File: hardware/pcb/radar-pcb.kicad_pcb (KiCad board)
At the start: 2 copper layers, 66 x 91 mm, 71 parts, among them J1 USB-C zasilanie 5 V (GCT USB4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, J10 Awaryjne wgrywanie: BOOT GND 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, J2 DevKit J1, J3 DevKit J3, J4 HC-SR04 (kabel): VCC TRIG ECH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, J5 Serwo SG90 (kabel): GND +5V S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, J6 MAX7219 Elegoo: VCC GND DIN C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, J7 OLED SH1106: VCC GND SCK SDA, J8 Buzzer: + -, J9 Przycisk zewnetrzny, Q2 MMBT3904, SW1 Przycisk ON/standby (katowy), U1 SN74AHCT125D, U2 AP22802AW5-7 (przelacznik 5 V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

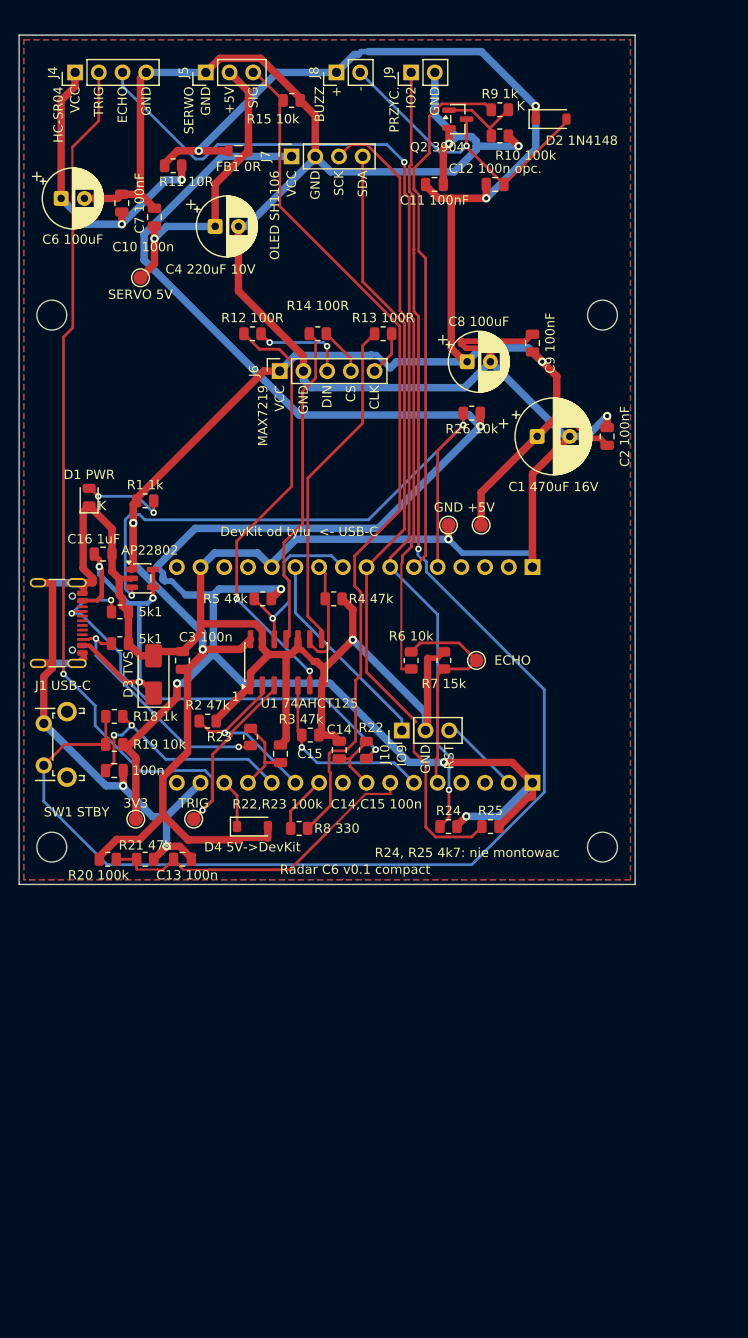
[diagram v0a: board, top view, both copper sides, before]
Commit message: PCB: USB-C zmienione na HRO TYPE-C-31-M-12 (LCSC C165948), BOM z C96346 dla 100 kΩ
GCT USB4105-GF-A był niedostępny w JLCPCB. Nowy footprint z biblioteki KiCad, gniazdo
przesunięte o 0,36 mm ku krawędzi (x = 2,74), usunięte dwa odcinki obrysu silkscreenu przy
krawędzi. Pełny build: ERC 0 błędów, DRC 0 błędów i 0 niepołączonych, 0 niezgodności ze
schematem, jedno ostrzeżenie lib_footprint_mismatch (celowa zmiana obrysu). Odświeżone rendery
i pliki produkcyjne. Nie sprawdzone na sprzęcie.

Co-Authored-By: Claude Sonnet 5.5 <noreply@anthropic.com>
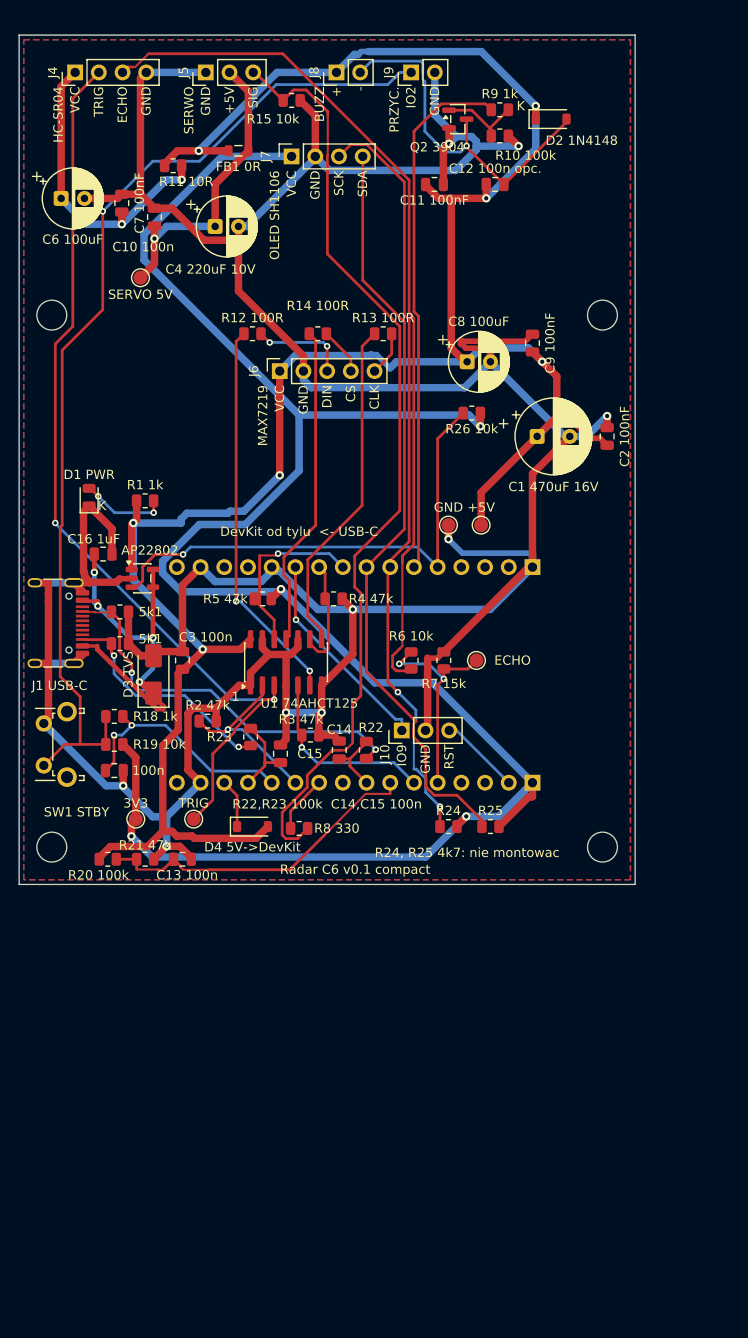
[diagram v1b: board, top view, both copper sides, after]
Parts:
- J1: value USB-C zasilanie 5 V (GCT USB4105) -> USB-C zasilanie 5 V (HRO TYPE-C-31-M-12); footprint Connector_USB:USB_C_Receptacle_GCT_USB4105-xx-A_16P_TopMnt_Horizontal -> Connector_USB:USB_C_Receptacle_HRO_TYPE-C-31-M-12
- moved J1 0.36 mm to (102.7, 88.0)
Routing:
- net BTN: track 157.4 -> 109.7 mm
- net U2_FLG: track 67.8 -> 54.0 mm, vias 2 -> 1
- net TRIG_5V: track 109.8 -> 100.0 mm
- net VIN: track 36.4 -> 45.6 mm, vias 3 -> 4
- net GND: track 418.2 -> 427.3 mm, vias 7 -> 9
- net SERVO_SIG: track 93.5 -> 101.3 mm
- net +5V: track 245.5 -> 252.4 mm, vias 6 -> 7
- net CC1: track 48.6 -> 42.3 mm, vias 3 -> 2
- net DIN_5V: track 46.8 -> 41.5 mm
- net BUZ_NEG: track 33.6 -> 38.8 mm
- net SDA: track 85.1 -> 82.1 mm
- net CC2: track 25.9 -> 24.6 mm
- net ECHO_3V3: track 24.7 -> 23.6 mm, vias 0 -> 2
- net +3V3: track 210.1 -> 209.1 mm, vias 5 -> 4
- net BUZ_CTRL: track 57.5 -> 56.9 mm
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
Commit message: PCB v0.2: wersja przewlekana (gniazdo DC, PTC + TVS, DIP-14), piny DevKita na listwach, pole prototypowe; firmware bez CC/FLG
Wszystko do ręcznego lutowania, płytki zamawiane bez montażu. Rozmieszczenie automatyczne
(tools/autoplace.py, geom.py), płytka 76 x 137,5 mm. J11/J12 = kopie wszystkich pinów DevKita,
J13 = listwa GND/3V3/5V, 4 bloki 2x14 = pole prototypowe. Miejsce na logo (footprint z Image Convertera)
w prawym dolnym rogu. POWER_MONITOR_USB_C=0 w firmware (tylko pomiar 5 V). Lista zakupów i Gerbery
w production/. ERC 0 błędów; DRC 0 błędów, 0 niepołączonych, 0 niezgodności ze schematem
(5 ostrzeżeń lib_footprint_mismatch: celowo uproszczone J1 i J14-J17). pio run przechodzi.
Nic nie sprawdzono na sprzęcie.

Co-Authored-By: Claude Sonnet 5.5 <noreply@anthropic.com>
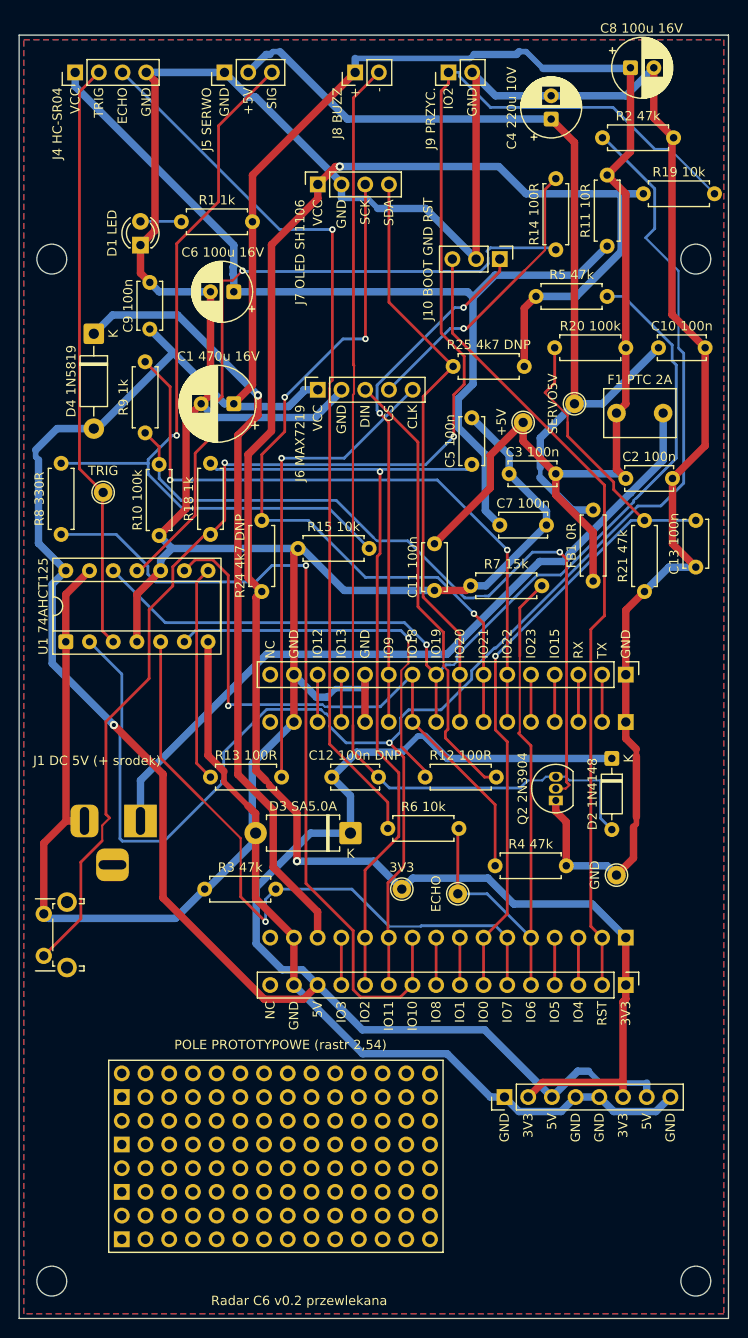
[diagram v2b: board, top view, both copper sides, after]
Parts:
- removed C14, C15: 100 nF, Capacitor_SMD:C_0805_2012Metric
- removed C16: 1 uF, Capacitor_SMD:C_0805_2012Metric
- removed R16, R17: 5,1 k, Resistor_SMD:R_0805_2012Metric
- removed R22, R23: 100 k, Resistor_SMD:R_0805_2012Metric
- removed R26: 10 k, Resistor_SMD:R_0805_2012Metric
- removed U2: AP22802AW5-7 (przelacznik 5 V, LCSC C211404, limit ok. 2,2-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, Package_TO_SOT_SMD:SOT-23-5
- added F1: PTC 2 A (hold), rastr 5 mm, Capacitor_THT:C_Disc_D7.5mm_W5.0mm_P5.00mm, F.Cu at (169.0, 65.5)
- added J11: Piny DevKit J3 (kopia J3), Connector_PinHeader_2.54mm:PinHeader_1x16_P2.54mm_Vertical, F.Cu at (165.0, 93.5)
- added J12: Piny DevKit J1 (kopia J2), Connector_PinHeader_2.54mm:PinHeader_1x16_P2.54mm_Vertical, F.Cu at (165.0, 126.8)
- added J13: Listwa zasilania: GND 3V3 5V, Connector_PinHeader_2.54mm:PinHeader_1x08_P2.54mm_Vertical, F.Cu at (152.0, 138.8)
- added J14: Pole prototypowe 1 (2x14, niepodlaczone), Connector_PinHeader_2.54mm:PinHeader_2x14_P2.54mm_Vertical, F.Cu at (111.0, 138.8)
- added J15: Pole prototypowe 2 (2x14, niepodlaczone), Connector_PinHeader_2.54mm:PinHeader_2x14_P2.54mm_Vertical, F.Cu at (111.0, 143.9)
- added J16: Pole prototypowe 3 (2x14, niepodlaczone), Connector_PinHeader_2.54mm:PinHeader_2x14_P2.54mm_Vertical, F.Cu at (111.0, 148.9)
- added J17: Pole prototypowe 4 (2x14, niepodlaczone), Connector_PinHeader_2.54mm:PinHeader_2x14_P2.54mm_Vertical, F.Cu at (111.0, 154.0)
- C10, C11, C12, C13, C2, C3, C5, C7, C9: footprint Capacitor_SMD:C_0805_2012Metric -> Capacitor_THT:C_Disc_D5.0mm_W2.5mm_P5.00mm
- D1: value LED zasilania -> LED zasilania 3 mm; footprint LED_SMD:LED_0805_2012Metric -> LED_THT:LED_D3.0mm
- D2: value 1N4148W -> 1N4148; footprint Diode_SMD:D_SOD-123 -> Diode_THT:D_DO-35_SOD27_P7.62mm_Horizontal
- D3: value SMAJ5.0A (TVS 5 V, jednokierunkowy) -> TVS SA5.0A (DO-15, katoda do +5V); footprint Diode_SMD:D_SMA -> Diode_THT:D_DO-15_P10.16mm_Horizontal
- D4: value 1N5819HW -> 1N5819; footprint Diode_SMD:D_SOD-123 -> Diode_THT:D_DO-41_SOD81_P10.16mm_Horizontal
- FB1: value 0 R (zworka; opcja: ferryt >= 1 A) -> 0 R (zworka z drutu; opcja: ferryt >= 1 A); footprint Inductor_SMD:L_0805_2012Metric -> Resistor_THT:R_Axial_DIN0207_L6.3mm_D2.5mm_P7.62mm_Horizontal
- J1: value USB-C zasilanie 5 V (HRO TYPE-C-31-M-12) -> Gniazdo DC 5,5/2,1 mm, srodek +5 V; footprint Connector_USB:USB_C_Receptacle_HRO_TYPE-C-31-M-12 -> Connector_BarrelJack:BarrelJack_Horizontal
- Q2: value MMBT3904 -> 2N3904 (TO-92, E B C); footprint Package_TO_SOT_SMD:SOT-23 -> Package_TO_SOT_THT:TO-92_Inline
- R1, R10, R11, R12, R13, R14, R15, R18, R19, R2, R20, R21, R24, R25, R3, R4, R5, R6, R7, R8, R9: footprint Resistor_SMD:R_0805_2012Metric -> Resistor_THT:R_Axial_DIN0207_L6.3mm_D2.5mm_P7.62mm_Horizontal
- TP1, TP2, TP3, TP4, TP5, TP6: footprint TestPoint:TestPoint_Pad_D1.5mm -> TestPoint:TestPoint_THTPad_D2.0mm_Drill1.0mm
- U1: value SN74AHCT125D -> SN74AHCT125N (DIP-14); footprint Package_SO:SOIC-14_3.9x8.7mm_P1.27mm -> Package_DIP:DIP-14_W7.62mm_Socket
- moved R19 87.3 mm to (174.5, 42.0), turned to 180 degrees
- moved R20 78.0 mm to (165.0, 58.5), turned to 180 degrees
- moved R2 75.5 mm to (162.5, 36.0)
- moved Q2 73.8 mm to (157.5, 107.0), turned to 90 degrees
- moved D2 68.8 mm to (163.5, 102.5), turned to -90 degrees
- moved C13 65.9 mm to (172.5, 77.0), turned to -90 degrees
- moved C12 65.9 mm to (133.5, 104.5)
- moved R21 64.7 mm to (167.0, 77.0), turned to -90 degrees
- moved FB1 59.7 mm to (161.5, 83.5), turned to 90 degrees
- moved C10 55.8 mm to (168.5, 58.5), turned to 0 degrees
- moved D4 55.5 mm to (108.0, 57.0), turned to -90 degrees
- moved C7 53.2 mm to (151.5, 77.5), turned to 0 degrees
- moved J10 51.6 mm to (151.5, 49.0), turned to -90 degrees
- moved R12 51.0 mm to (143.5, 104.5)
- moved R13 51.0 mm to (120.5, 104.5)
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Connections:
- D3 pad 1: VIN -> +5V
- J2 pad 13: CC2_SENSE -> IO3
- J2 pad 3: unconnected-(J2-Pin_3-Pad3) -> IO4
- J2 pad 4: unconnected-(J2-Pin_4-Pad4) -> IO5
- J2 pad 8: CC1_SENSE -> IO1
- J2 pad 9: unconnected-(J2-Pin_9-Pad9) -> IO8
- J3 pad 13: unconnected-(J3-Pin_13-Pad13) -> IO13
- J3 pad 14: unconnected-(J3-Pin_14-Pad14) -> IO12
- J3 pad 2: unconnected-(J3-Pin_2-Pad2) -> TX
- J3 pad 3: unconnected-(J3-Pin_3-Pad3) -> RX
- J3 pad 4: unconnected-(J3-Pin_4-Pad4) -> IO15
- J3 pad 5: U2_FLG -> IO23
- Q2 pad 1: BUZ_BASE -> GND
- Q2 pad 2: GND -> BUZ_BASE
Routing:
- net TRIG_3V3: track 19.5 -> 174.7 mm
- net +5V: track 252.4 -> 392.3 mm, vias 7 -> 1
- net GND: track 427.3 -> 551.4 mm, vias 9 -> 0
- net SERVO_3V3: track 6.16 -> 89.4 mm, vias 0 -> 1
- net CS_3V3: track 19.8 -> 102.8 mm
- net DEVKIT_5V: track 5.27 -> 84.5 mm, vias 0 -> 1
- net EN: track 8.70 -> 85.6 mm
- net BUZ_BASE: track 8.85 -> 82.7 mm, vias 0 -> 1
- net BUZ_NEG: track 38.8 -> 108.6 mm, vias 1 -> 0
- net SR04_VCC: track 33.0 -> 100.0 mm, vias 2 -> 0
- net SERVO_5V: track 32.0 -> 96.0 mm, vias 1 -> 0
- net BTN_ESP: track 25.4 -> 86.3 mm, vias 2 -> 1
- net U2_FLG: track 54.0 -> 0.00 mm, vias 1 -> 0
- net CLK_3V3: track 12.1 -> 65.3 mm, vias 0 -> 1
- net BTN: track 109.7 -> 162.4 mm, vias 1 -> 2
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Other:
- board size 66 x 91 mm -> 76 x 137.5 mm
- board text added: "C1 470u 16V"
- board text added: "C11 100n"
- board text added: "C12 100n DNP"
- board text added: "C2 100n"
- board text added: "C4 220u 10V"
- board text added: "C5 100n"
- board text added: "C6 100u 16V"
- board text added: "C7 100n"
- board text added: "C8 100u 16V"
- board text added: "C9 100n"
- board text added: "D1 LED"
- board text added: "D3 SA5.0A"
- board text added: "D4 1N5819"
- board text added: "F1 PTC 2A"
- board text added: "J1 DC 5V (+ srodek)"
- board text added: "J10 BOOT GND RST"
- board text added: "J4 HC-SR04"
- board text added: "J5 SERWO"
- board text added: "J6 MAX7219"
- board text added: "J7 OLED SH1106"
- board text added: "J8 BUZZ"
- board text added: "J9 PRZYC."
- board text added: "POLE PROTOTYPOWE (rastr 2,54)"
- board text added: "Projekt roboczy v0.2 (przewlekany) - NIE ZAMAWIAC przed weryfikacja wymiarow."
- board text added: "Q2 2N3904"
- board text added: "R24 4k7 DNP"
- board text added: "R25 4k7 DNP"
- board text added: "R8 330R"
- board text added: "Radar C6 v0.2 przewlekana"
- board text added: "Radar ESP32-C6 - tyl, DevKit USB-C ->"
- board text added: "SERVO5V"
- board text added: "W1 szerokosc plytki: czy miesci sie we wnetrzu obudowy"
- board text added: "W2 wysokosc plytki (wersja przewlekana, z polem prototypowym)"
- board text added: "W6 gniazdo DC: od gornej krawedzi do osi wtyku (otwor w scianie obudowy)"
- board text added: "WYMIARY DO WERYFIKACJI (? = do potwierdzenia, OK = zmierzone)"
- board text removed: "1"
- board text removed: "100n"
- board text removed: "5k1"
- board text removed: "AP22802"
- board text removed: "BUZZ"
- board text removed: "C1 470uF 16V"
- board text removed: "C11 100nF"
- board text removed: "C12 100n opc."
- board text removed: "C14"
- board text removed: "C15"
- board text removed: "C16 1uF"
- board text removed: "C2 100nF"
- board text removed: "C4 220uF 10V"
- board text removed: "C6 100uF"
- board text removed: "C7 100nF"
- board text removed: "C8 100uF"
- board text removed: "C9 100nF"
- board text removed: "D1 PWR"
- board text removed: "D3 TVS"
- board text removed: "D4 5V->DevKit"
- board text removed: "DevKit J1 (pin 1 = 3V3)"
- board text removed: "DevKit J3 (pin 1 = GND)"
- board text removed: "DevKit od tylu <- USB-C"
- board text removed: "HC-SR04"
- board text removed: "J1 USB-C"
- board text removed: "J10"
- board text removed: "K"
- board text removed: "MAX7219"
- board text removed: "OLED SH1106"
- board text removed: "PRZYC."
- board text removed: "Projekt roboczy v0.1 - NIE ZAMAWIAC przed weryfikacja wymiarow."
- board text removed: "Q2 3904"
- board text removed: "R22"
- board text removed: "R22,R23 100k C14,C15 100n"
- board text removed: "R23"
- board text removed: "R24"
- board text removed: "R24, R25 4k7: nie montowac"
- board text removed: "R25"
- board text removed: "R26 10k"
- board text removed: "R8 330"
- board text removed: "Radar C6 v0.1 compact"
- board text removed: "Radar ESP32-C6 - tyl"
- board text removed: "SERVO 5V"
- board text removed: "SERWO"
- board text removed: "SW1 STBY"
- board text removed: "USB-C ->"
- board text removed: "W1 szerokosc plytki: czy miesci sie we wnetrzu kolumny obudowy"
- board text removed: "W2 wysokosc plytki (wariant kompaktowy, moduly na kablach)"
- board text removed: "W3 gniazdo kabla OLED (J7): od lewej krawedzi do pinu 1"
- board text removed: "W4 gniazdo kabla MAX7219 (J6): od lewej krawedzi do pinu 1"
- board text removed: "W6 gniazdo USB-C zasilania: od gornej krawedzi do osi wtyku (otwor w scianie obudowy)"
- board text removed: "WYMIARY DO WERYFIKACJI (? = do potwierdzenia, OK = zmierzone lub zatwierdzone 2026-10-13)"

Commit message: PCB v0.2: logo Adam & Mateusz na silkscreenie (prawy dolny róg)
logo_trace.py wektoryzuje logo/am-logo-source.jfif (kontury, gładkie krawędzie, otwory w literach),
logo_footprint.py zapisuje footprint logo/am-logo.kicad_mod na F.SilkS (odpowiednik Image Convertera),
gen_pcb.py ustawia go w obszarze G.LOGO. Płytka 76 x 137,5 mm, DRC bez błędów (0 niepołączonych).
Odświeżone rendery i Gerbery. Nic nie sprawdzono na sprzęcie.

Co-Authored-By: Claude Sonnet 5.5 <noreply@anthropic.com>
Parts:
- added LOGO: am-logo, am-logo, F.Cu at (158.0, 153.4)

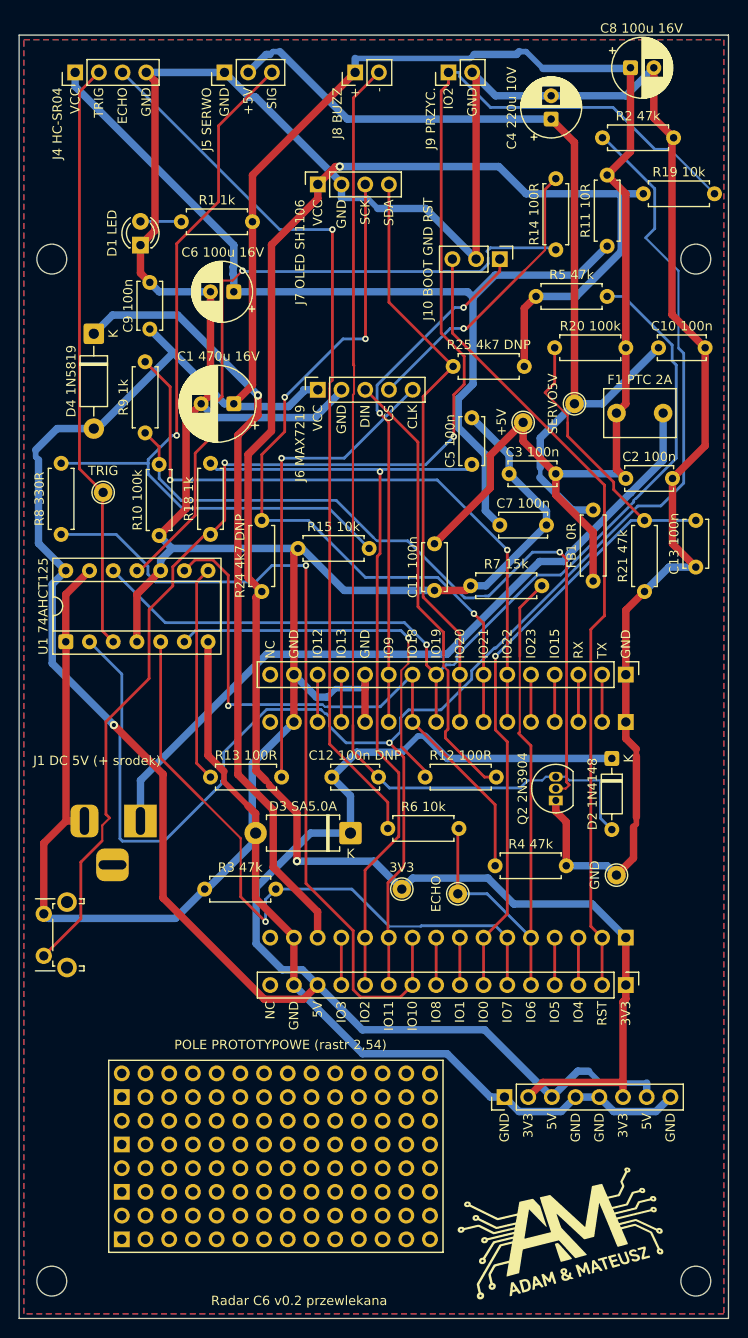
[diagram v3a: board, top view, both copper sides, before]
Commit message: PCB v0.2: wszystkie listwy żeńskie (J4-J13)
Listwy J4, J5, J8, J9, J10, J11, J12 i J13 zmienione z goldpinów na gniazda żeńskie (ten sam rozstaw
i numeracja pinów, układ i trasowanie bez zmian). Lista zakupów i notatki zaktualizowane.
ERC 0 błędów; DRC 0 błędów, 0 niepołączonych, 0 niezgodności ze schematem. Nic nie sprawdzono na sprzęcie.

Co-Authored-By: Claude Sonnet 5.5 <noreply@anthropic.com>
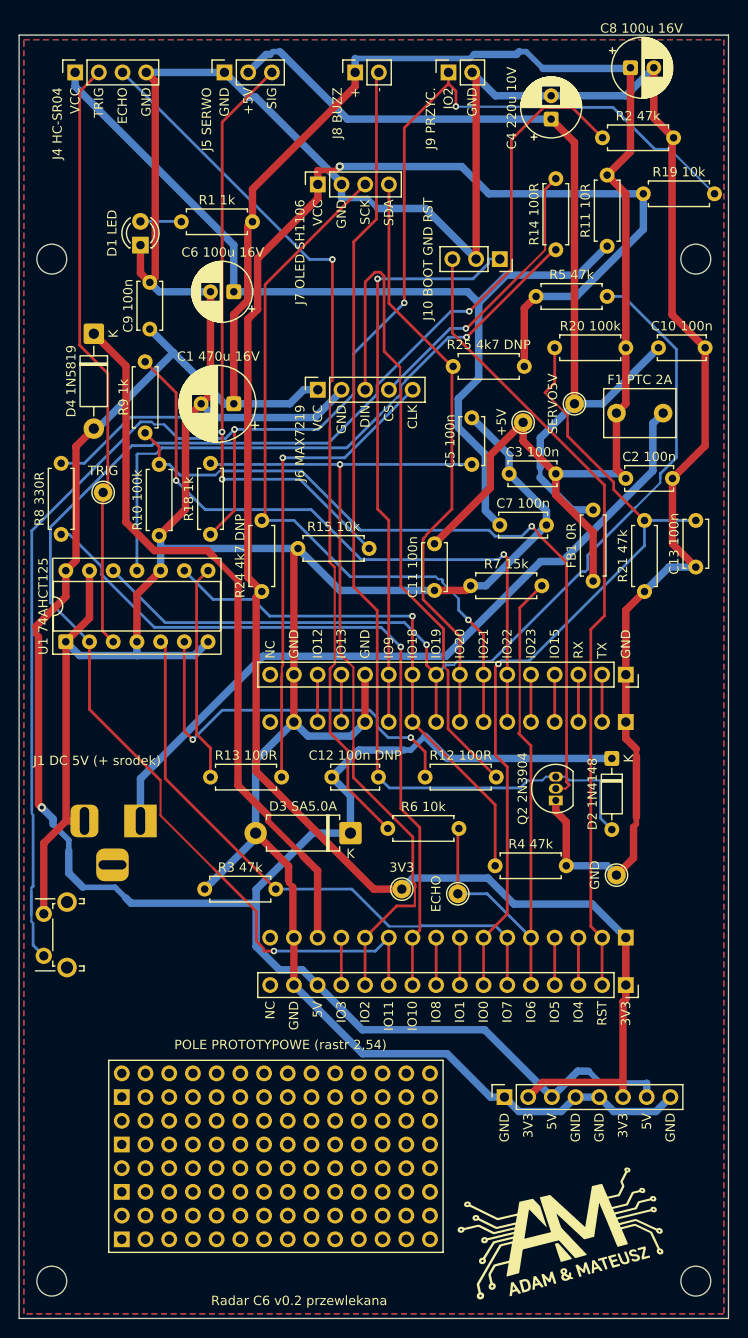
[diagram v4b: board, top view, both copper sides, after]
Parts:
- J10, J5: footprint Connector_PinHeader_2.54mm:PinHeader_1x03_P2.54mm_Vertical -> Connector_PinSocket_2.54mm:PinSocket_1x03_P2.54mm_Vertical
- J11, J12: footprint Connector_PinHeader_2.54mm:PinHeader_1x16_P2.54mm_Vertical -> Connector_PinSocket_2.54mm:PinSocket_1x16_P2.54mm_Vertical
- J13: footprint Connector_PinHeader_2.54mm:PinHeader_1x08_P2.54mm_Vertical -> Connector_PinSocket_2.54mm:PinSocket_1x08_P2.54mm_Vertical
- J4: footprint Connector_PinHeader_2.54mm:PinHeader_1x04_P2.54mm_Vertical -> Connector_PinSocket_2.54mm:PinSocket_1x04_P2.54mm_Vertical
- J8, J9: footprint Connector_PinHeader_2.54mm:PinHeader_1x02_P2.54mm_Vertical -> Connector_PinSocket_2.54mm:PinSocket_1x02_P2.54mm_Vertical
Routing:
- net DIN_J: track 48.3 -> 72.8 mm
- net GND: track 551.4 -> 529.7 mm
- net TRIG_3V3: track 174.7 -> 161.7 mm, vias 1 -> 2
- net BTN: track 162.4 -> 173.6 mm, vias 2 -> 3
- net +5V: track 392.3 -> 381.4 mm
- net SERVO_3V3: track 89.4 -> 79.3 mm
- net CLK_3V3: track 65.3 -> 56.9 mm
- net DIN_3V3: track 70.7 -> 63.7 mm, vias 1 -> 0
- net DEVKIT_5V: track 84.5 -> 78.0 mm, vias 1 -> 0
- net CS_5V: track 73.4 -> 67.0 mm
- net BOOT: track 56.1 -> 62.2 mm, vias 2 -> 1
- net BTN_ESP: track 86.3 -> 90.5 mm
- net BUZ_BASE: track 82.7 -> 78.9 mm
- net ECHO_5V: track 96.3 -> 94.8 mm
- net SCL: track 80.9 -> 79.6 mm, vias 3 -> 1
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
